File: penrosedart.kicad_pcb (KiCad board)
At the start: 2 copper layers, 50 x 47.5 mm, 19 parts, among them J1 Conn_01x03_Female, J2 Conn_01x03_Female, J3 Conn_01x03_Male, J4 Conn_01x03_Male, M2.1 MountingHole_2.1mm, SW1 SW_DPDT_x2

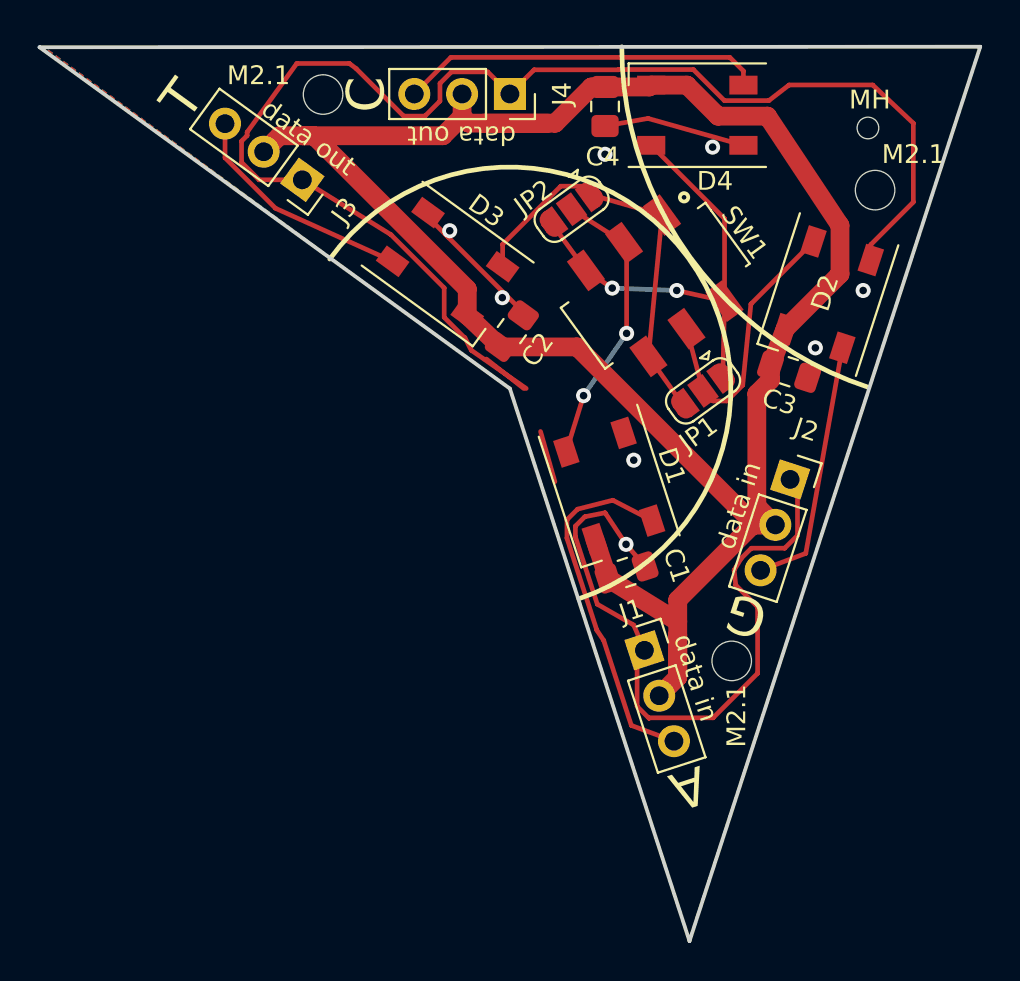
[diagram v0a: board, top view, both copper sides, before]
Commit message: shifted ports  on penrose rhombi to enforce all matching rules. fixed flipped ports on penrose dart.
going to make new gerbers later.
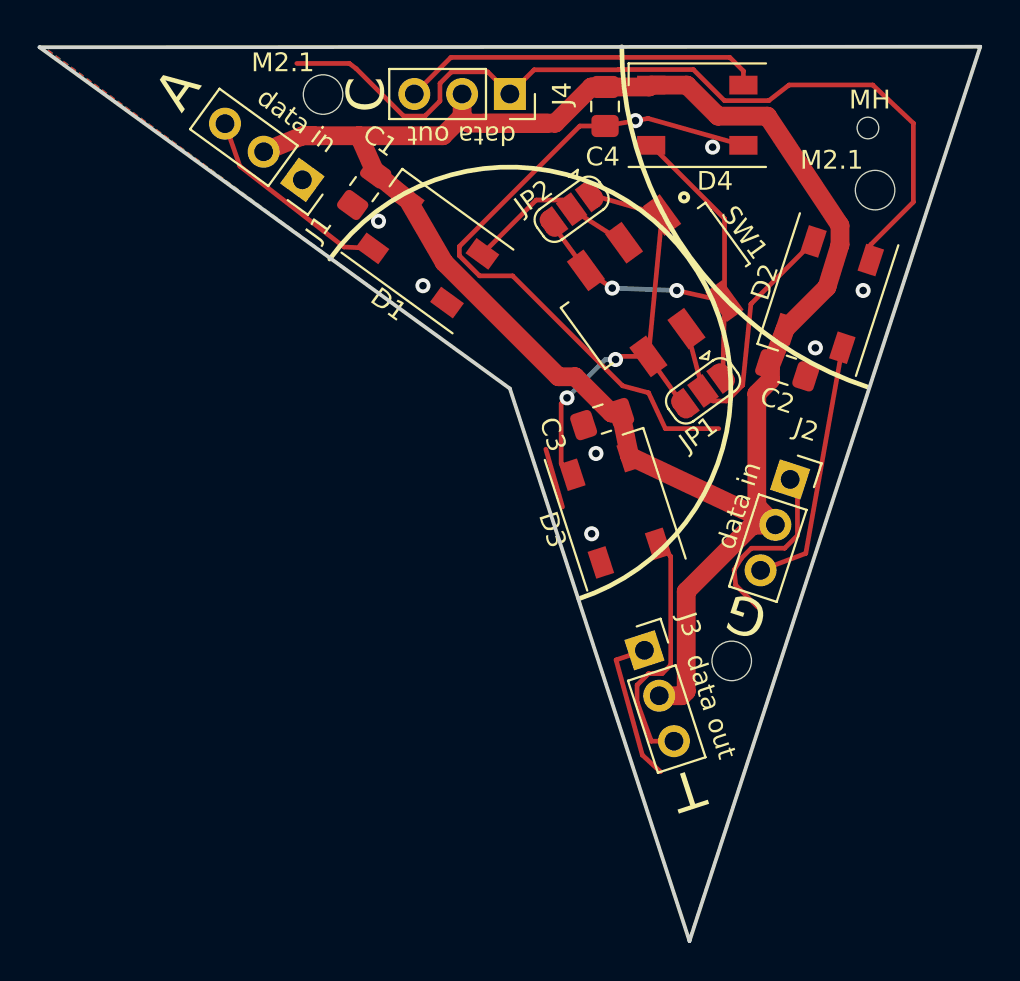
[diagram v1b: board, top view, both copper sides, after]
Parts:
-  : renamed from M2.1
- moved J1 30.9 mm to (139.4, 81.2), turned to 234 degrees
- moved J3 30.9 mm to (157.5, 106.2), turned to 18 degrees
- moved C1 24.7 mm to (142.6, 81.7), turned to 54 degrees
- moved D1 15.8 mm to (146.0, 85.0), turned to 144 degrees
- moved D3 15.8 mm to (156.0, 98.7), turned to 108 degrees
- moved C2 14.8 mm to (165.1, 91.4), turned to 162 degrees
- moved C3 10.2 mm to (155.3, 94.0), turned to 18 degrees
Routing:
- net GND: track 131.4 -> 104.1 mm
- net VCC: track 114.5 -> 105.0 mm
- net Net-(D1-Pad2): track 19.0 -> 10.9 mm
- net Net-(D1-Pad4): track 15.3 -> 9.43 mm, vias 2 -> 0
- net Net-(D3-Pad2): track 22.0 -> 24.3 mm, vias 0 -> 2
- net Net-(D3-Pad4): track 12.4 -> 13.3 mm
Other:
- board text added: "GND VCC DATA"
- board text added: "Gnd 5v Data"

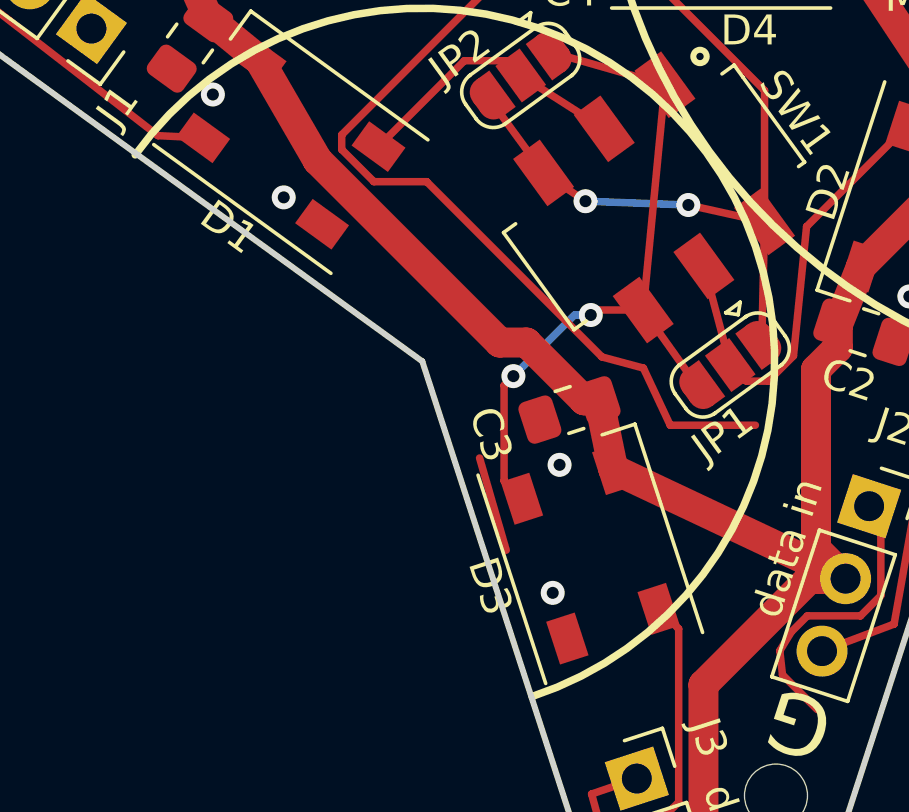
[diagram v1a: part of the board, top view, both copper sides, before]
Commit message: updated gerbers and images. new gerbers of rombi now enforce the tiling rules by making ports misalign when.
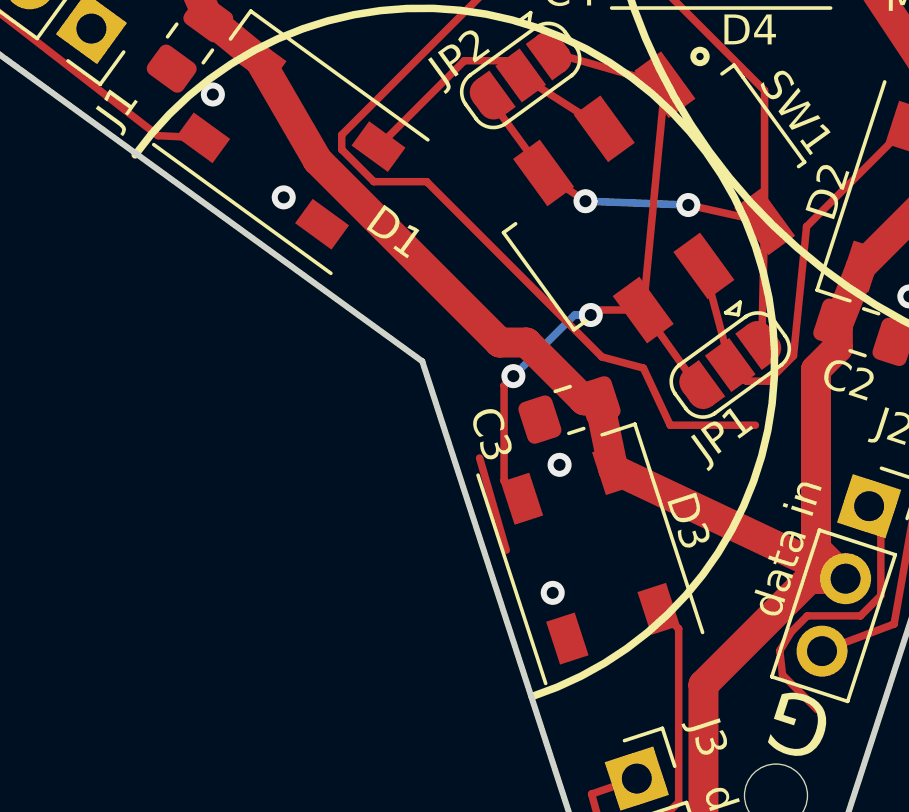
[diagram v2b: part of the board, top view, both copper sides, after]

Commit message: increased mounting hole size to M3
increased mounting hole size to M3 to accomidate plastic adhesive mounting hole standoffs. makes the silkscreen a bit cramped and the VCC   route a bit long, but maybe I will make the top pour VCC instead of ground later idk.
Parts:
- added M3: MountingHole_3.2mm_M3_ISO7380, MountingHole:MountingHole_3.2mm_M3_ISO7380, F.Cu at (152.2, 90.5)
- M3: renamed from  ; value MountingHole_2.1mm -> MountingHole_3.2mm_M3_ISO7380; footprint MountingHole:MountingHole_2.1mm -> MountingHole:MountingHole_3.2mm_M3_ISO7380
- M3 (x2): renamed from M2.1; value MountingHole_2.1mm -> MountingHole_3.2mm_M3_ISO7380; footprint MountingHole:MountingHole_2.1mm -> MountingHole:MountingHole_3.2mm_M3_ISO7380
- moved M3 3.17 mm to (167.0, 80.2)
- moved JP1 0.85 mm to (160.8, 91.6)
- moved M3 0.59 mm to (162.0, 106.2)
- moved M3 0.55 mm to (140.9, 77.0)
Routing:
- net GND: track 104.1 -> 78.4 mm, vias 8 -> 10
- net VCC: track 105.0 -> 107.1 mm
- net Net-(D2-Pad4): track 15.1 -> 13.1 mm
- net Net-(D3-Pad4): track 13.3 -> 11.5 mm, vias 0 -> 1
- net Net-(D4-Pad2): track 24.7 -> 23.9 mm
- net Net-(D3-Pad2): track 24.3 -> 23.8 mm

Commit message: updated penrose dart with powerplane
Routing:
- net GND: track 78.4 -> 50.4 mm, vias 10 -> 0
- net VCC: track 107.1 -> 115.5 mm
- net Net-(D4-Pad4): track 19.3 -> 24.3 mm
- net Net-(D3-Pad4): track 11.5 -> 16.1 mm, vias 1 -> 0
- net Net-(D4-Pad2): track 23.9 -> 23.2 mm, vias 2 -> 3
- added copper zone on F.Cu, net VCC
- removed copper zone on F.Cu, net GND

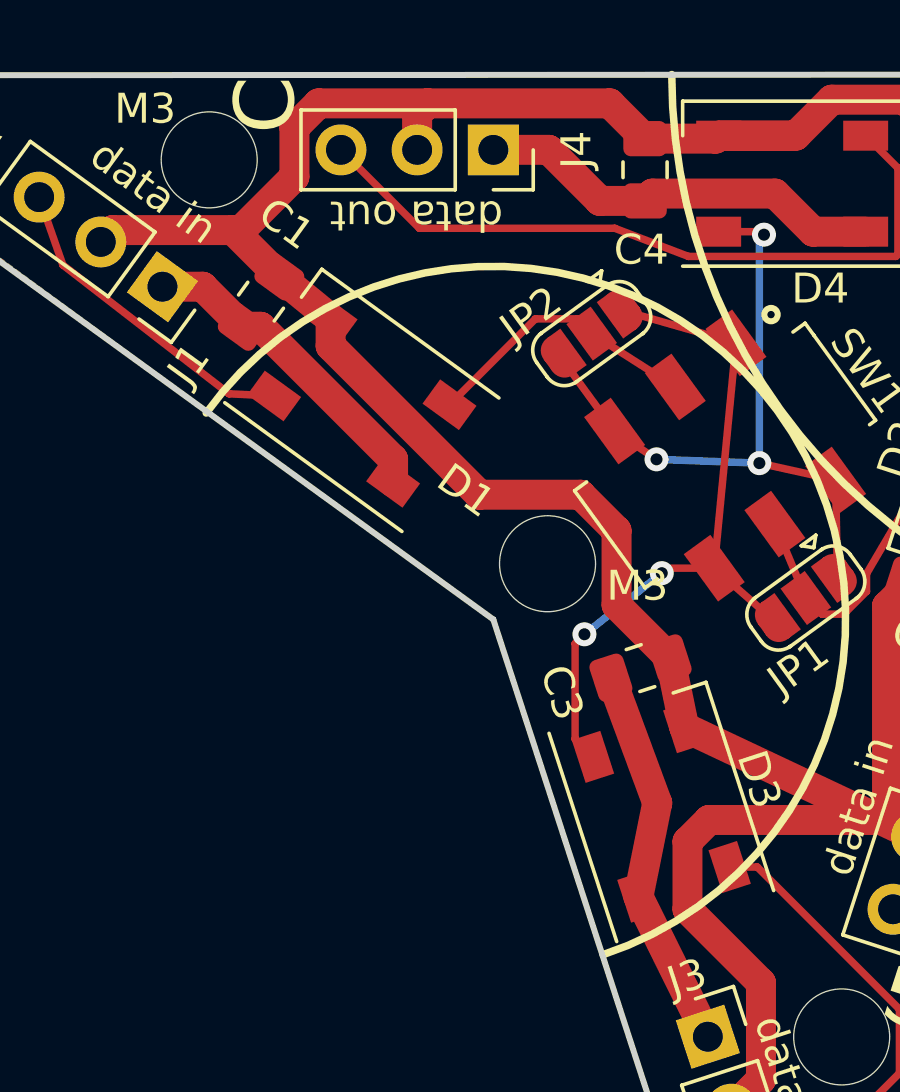
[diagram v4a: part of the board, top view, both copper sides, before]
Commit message: board wiring changes and mounting hole additions for adhesive standoffs
changed top copper fill to VCC and added mounting holes with new footprint to check if the mounts collided.
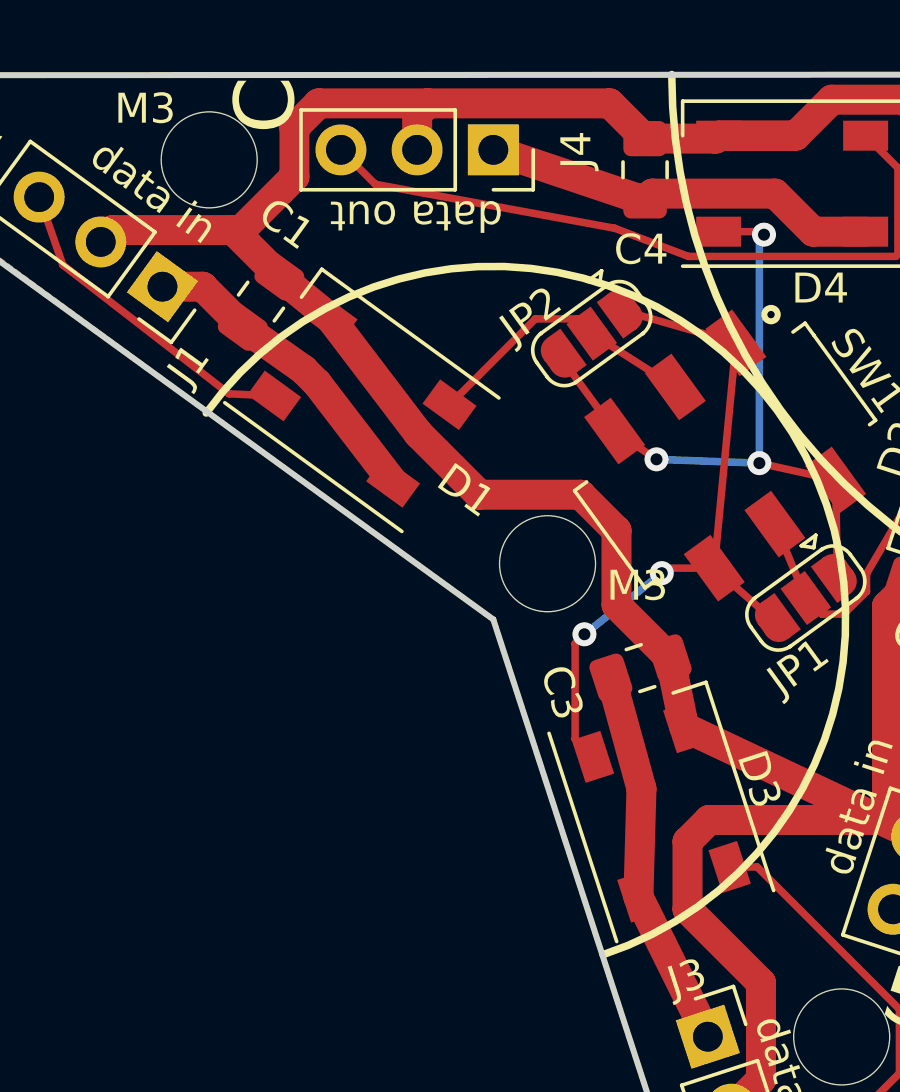
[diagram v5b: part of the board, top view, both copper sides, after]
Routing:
- net GND: track 50.4 -> 49.5 mm

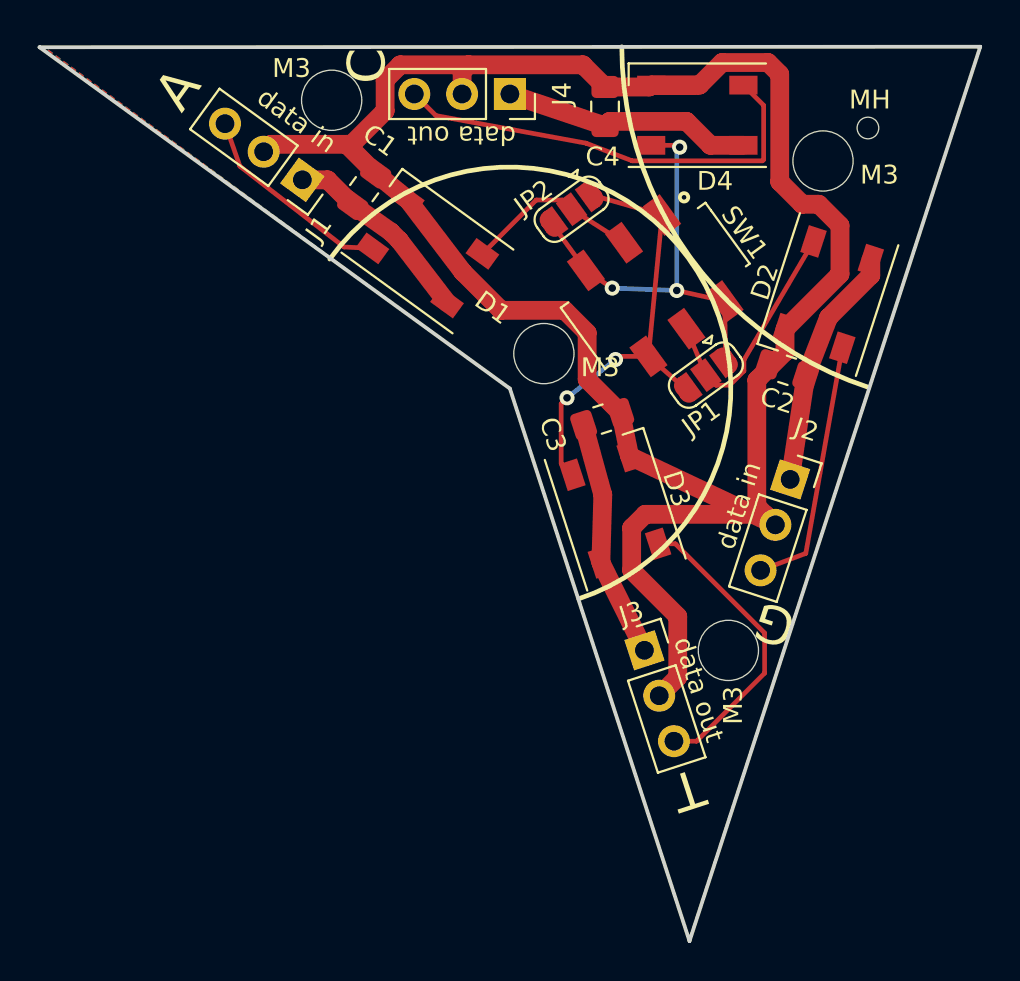
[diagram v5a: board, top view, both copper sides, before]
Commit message: minor tweaks and diagrams
Tweaks to silkscreen and stuff also added a diagram to explain switch on board. Also made top layer VCC on penrose kite.
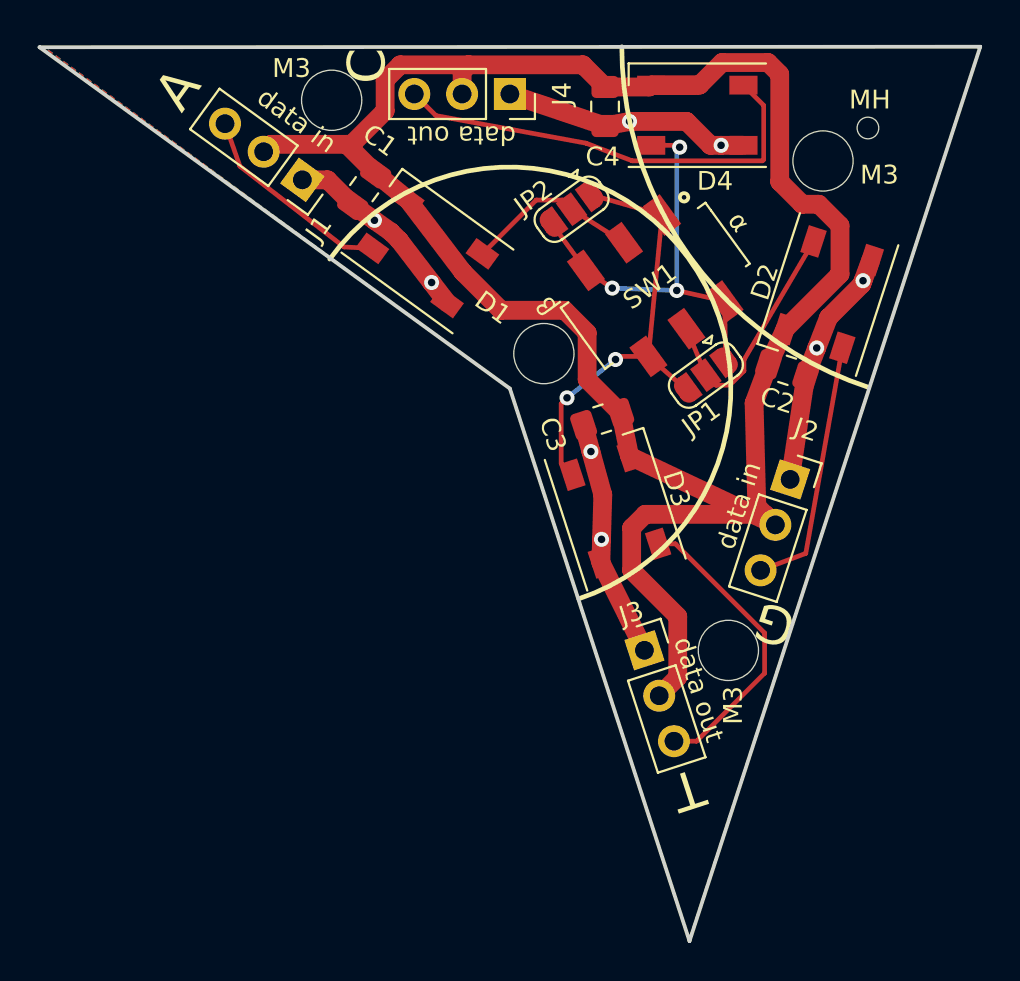
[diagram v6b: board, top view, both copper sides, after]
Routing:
- net GND: track 49.5 -> 49.3 mm, vias 0 -> 8
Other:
- board text added: "α"
- board text added: "β"
